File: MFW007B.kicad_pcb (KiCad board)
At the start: 4 copper layers, 84 x 42 mm, 96 parts, among them J1 Conn_01x04, J2 Conn_02x07, J3 4P JST-SH, J4 Conn_02x03, SW2 SW_Push, SW3 SW_Push, SW4 SW_Push, U1 24AA02-OT, U2 W5500, U3 STM32F103C8T6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

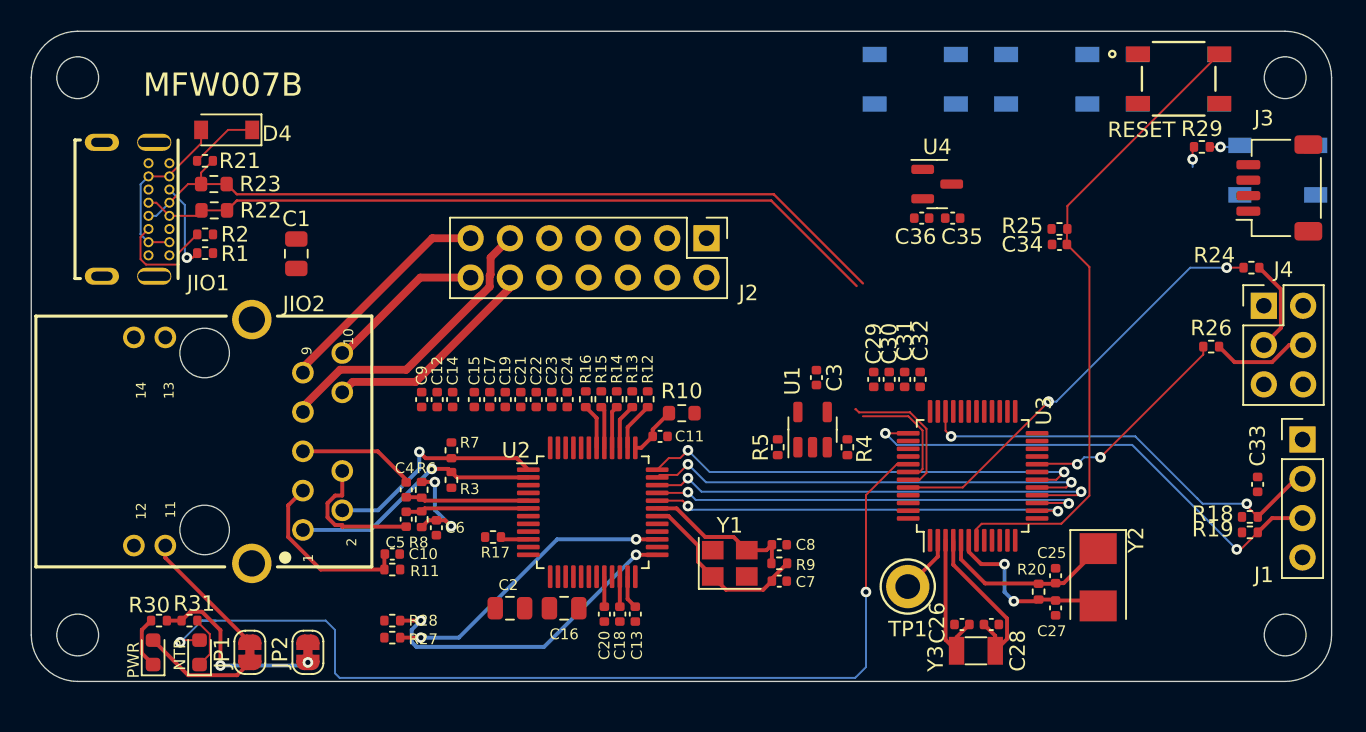
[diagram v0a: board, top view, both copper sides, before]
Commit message: add gnd + 3.3v fills
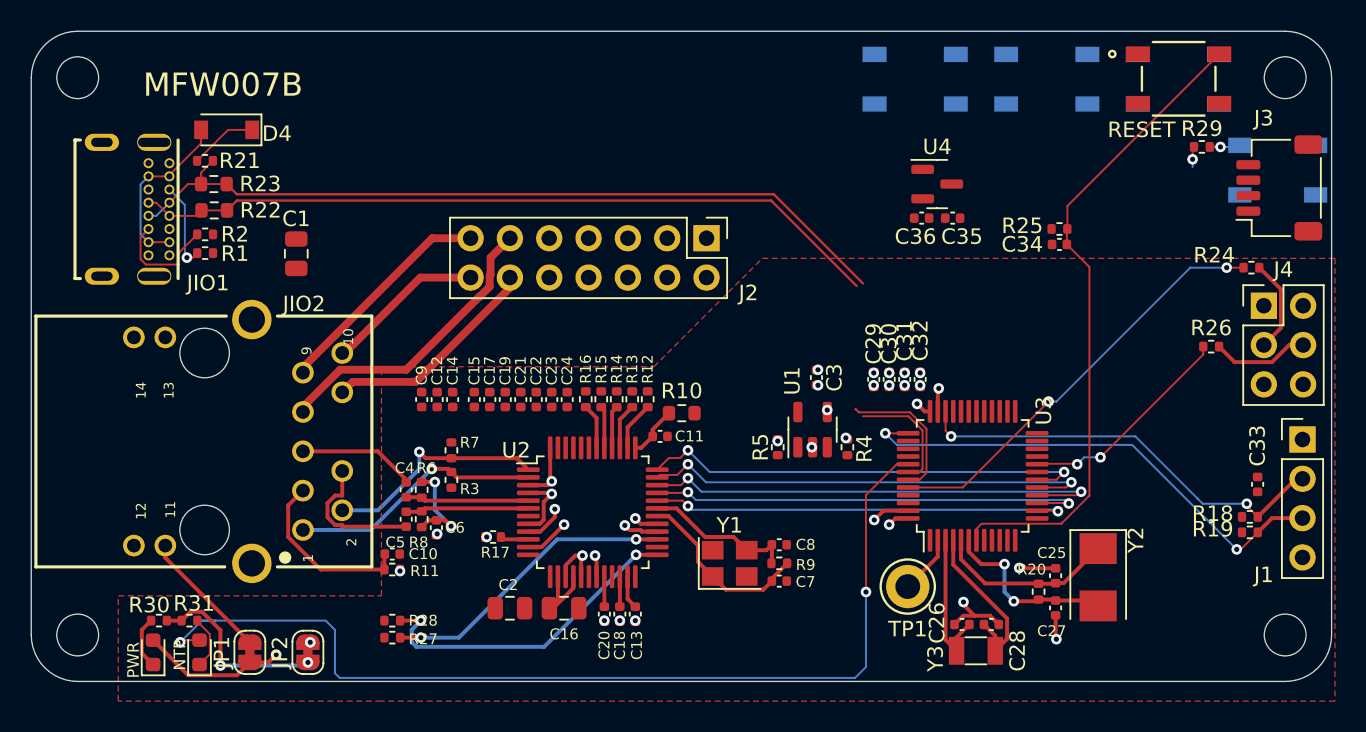
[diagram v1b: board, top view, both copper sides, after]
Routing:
- net GND: track 0.00 -> 26.9 mm, vias 0 -> 21
- net +3V3: track 7.53 -> 25.1 mm, vias 0 -> 16
- added copper zone on F.Cu, net +3V3
- added copper zone on In1.Cu, net GND

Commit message: connect to planes
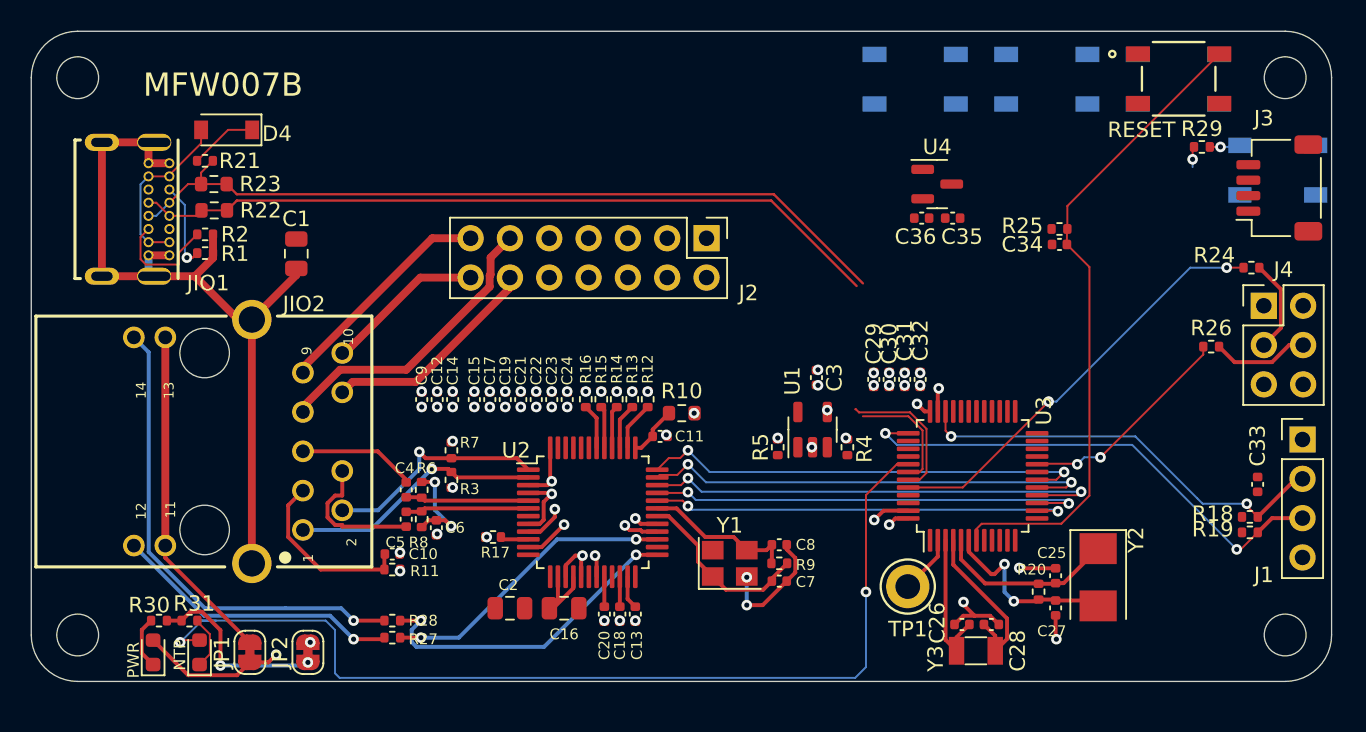
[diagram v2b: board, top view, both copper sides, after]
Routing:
- net GND: track 26.9 -> 86.7 mm, vias 21 -> 40
- net Net-(JIO2-Pad14): track 0.00 -> 31.3 mm, vias 0 -> 1
- net Net-(JIO2-Pad12): track 0.00 -> 18.7 mm, vias 0 -> 1
- net Net-(JIO2-Pad11): track 8.51 -> 22.0 mm
- net /MCU/OSC_OUT: track 11.7 -> 12.2 mm
- net +3V3: vias 16 -> 29
- added copper zone on In2.Cu, net +3V3
- removed copper zone on F.Cu, net +3V3

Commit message: more routing
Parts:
- moved C34 3.22 mm to (156.2, 95.8)
- moved R25 3.22 mm to (156.2, 94.8)
- moved R21 2.20 mm to (101.8, 87.5)
- moved C29 1.00 mm to (141.8, 101.6)
- moved C30 1.00 mm to (142.8, 101.6)
- moved C31 1.00 mm to (143.8, 101.6)
- moved C32 1.00 mm to (144.8, 101.6)
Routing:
- net /I2C1_SDA: track 9.35 -> 47.4 mm, vias 0 -> 2
- net /I2C1_SCL: track 7.74 -> 42.8 mm, vias 0 -> 2
- net /RGB_LED: track 1.34 -> 31.6 mm, vias 1 -> 4
- net /USER_SW_3: track 0.00 -> 29.1 mm, vias 0 -> 1
- net /USER_SW_1: track 0.00 -> 27.3 mm, vias 0 -> 1
- net /I2C2_SCL: track 0.00 -> 26.4 mm
- net /USER_SW_2: track 0.00 -> 25.2 mm, vias 0 -> 1
- net /I2C2_SDA: track 0.00 -> 25.2 mm
- net /SPI2_SCK: track 0.00 -> 19.0 mm
- net /SPI2_CS: track 0.00 -> 18.9 mm
- net /SPI2_MISO: track 0.00 -> 18.6 mm
- net /SPI2_MOSI: track 0.00 -> 18.4 mm
- net GND: track 86.7 -> 104.6 mm, vias 40 -> 51
- net /USBDN: track 48.8 -> 62.4 mm, vias 0 -> 2
- net /USBDP: track 51.5 -> 64.4 mm, vias 0 -> 2
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- added copper zone on In2.Cu, net +5V

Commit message: finetune routing
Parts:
- moved C29 0.89 mm to (142.6, 101.2)
- moved C30 0.89 mm to (143.6, 101.2)
- moved C31 0.89 mm to (144.6, 101.2)
- moved C32 0.89 mm to (145.6, 101.2)
- moved R18 0.50 mm to (167.1, 111.0)
- moved R19 0.50 mm to (167.1, 112.0)
- moved J1 0.20 mm to (170.5, 105.7)
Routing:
- net /I2C1_SCL: track 42.8 -> 65.5 mm
- net /SPI2_MISO: track 18.6 -> 36.7 mm
- net /I2C1_SDA: track 47.4 -> 64.1 mm, vias 2 -> 3
- net /SPI2_CS: track 18.9 -> 35.6 mm
- net /SPI2_MOSI: track 18.4 -> 34.4 mm
- net /SPI2_SCK: track 19.0 -> 33.0 mm
- net /I2C2_SCL: track 26.4 -> 39.6 mm
- net /I2C2_SDA: track 25.2 -> 37.0 mm
- net +3V3: track 32.2 -> 33.9 mm
- net GND: track 104.6 -> 106.3 mm
- net /MCU/SWCLK: track 33.1 -> 33.8 mm
- net /MCU/SWO: track 27.7 -> 28.4 mm

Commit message: fix DRC
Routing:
- net +3V3: track 33.9 -> 35.3 mm

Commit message: order PCB
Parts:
- moved C12 1.01 mm to (115.0, 103.8)
- moved C14 1.01 mm to (116.0, 103.8)
- moved C9 1.01 mm to (114.0, 103.8)
- moved C15 0.90 mm to (117.0, 103.8)
- moved C17 0.90 mm to (118.0, 103.8)
- moved C19 0.90 mm to (119.0, 103.8)
- moved C21 0.90 mm to (120.0, 103.8)
- moved C22 0.90 mm to (121.0, 103.8)
- moved C23 0.90 mm to (122.0, 103.8)
- moved C24 0.90 mm to (123.0, 103.8)
- renumbered RESET to SW1
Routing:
- net +3V3: track 35.3 -> 41.0 mm
- net /USER_SW_3: track 29.1 -> 28.4 mm
- net GND: vias 51 -> 53
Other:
- board text added: "RESET"

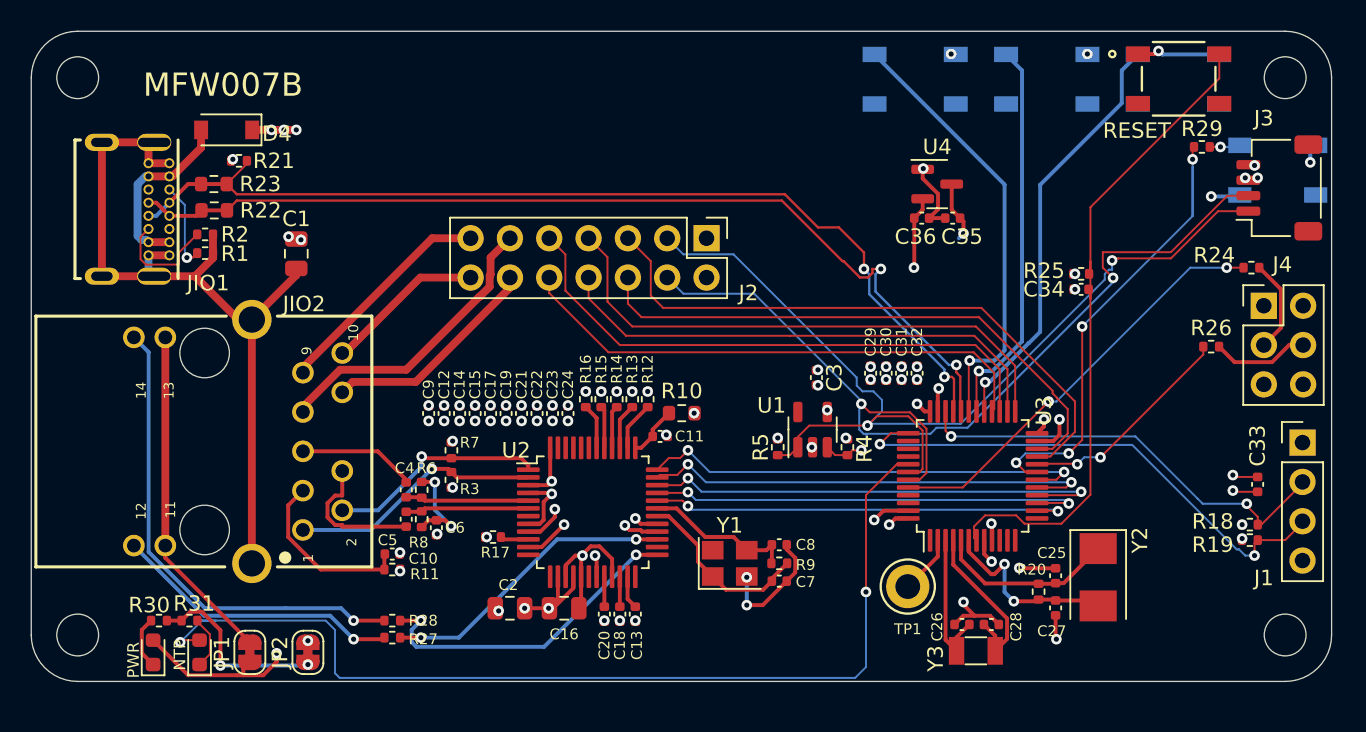
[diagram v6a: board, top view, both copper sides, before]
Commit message: fix vias
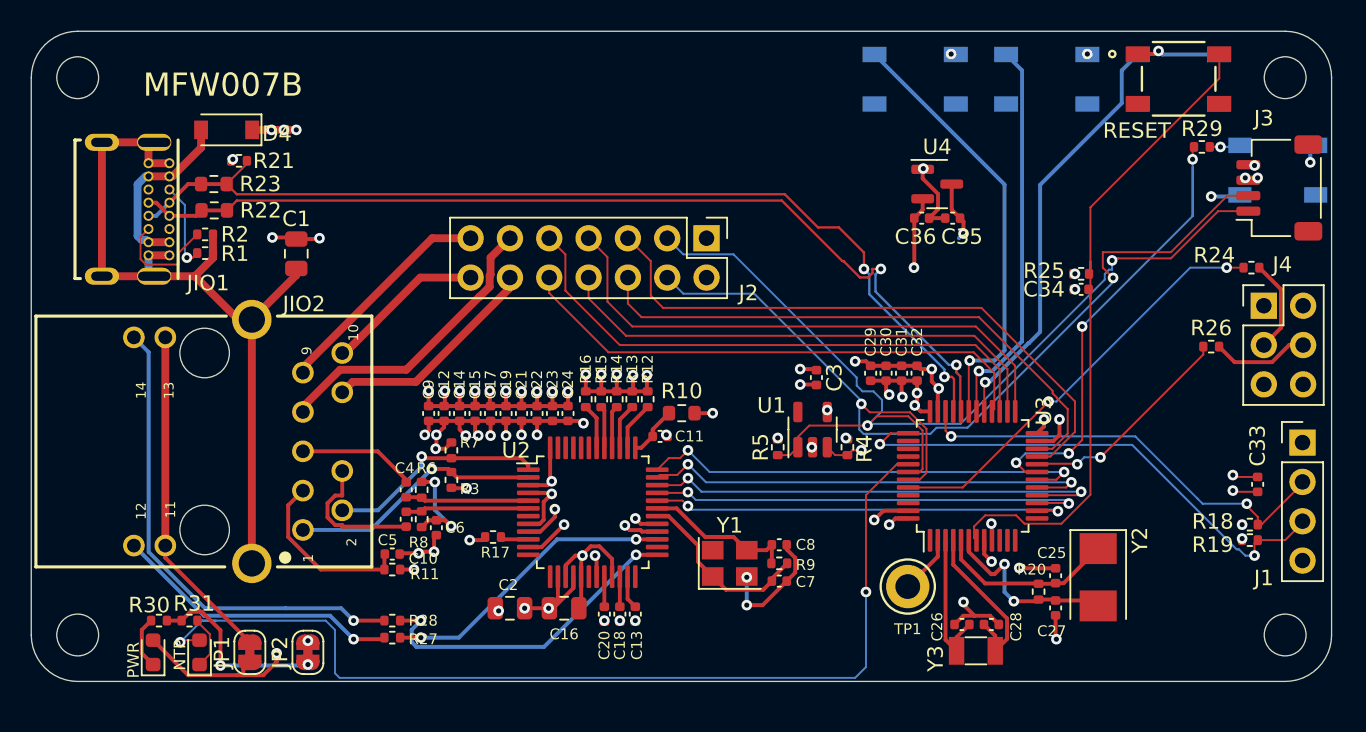
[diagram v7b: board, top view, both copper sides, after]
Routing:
- net GND: track 106.3 -> 146.6 mm, vias 53 -> 51
- net +3V3: track 41.0 -> 72.1 mm, vias 36 -> 34
- net +5V: track 8.04 -> 11.1 mm
